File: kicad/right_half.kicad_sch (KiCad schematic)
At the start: 50 parts, among them J10 Conn_01x03_Pin, J3 AudioJack4, J4 Conn_01x04_Pin, J9 Conn_01x04_Pin, SW19 SW_Push, SW20 SW_Push, SW21 SW_Push, SW22 SW_Push, SW23 SW_Push, SW24 SW_Push, SW25 SW_Push, SW26 SW_Push, SW27 SW_Push, SW28 SW_Push, SW29 SW_Push, SW30 SW_Push, SW31 SW_Push, SW32 SW_Push, SW33 SW_Push, U2 RP2040-Zero

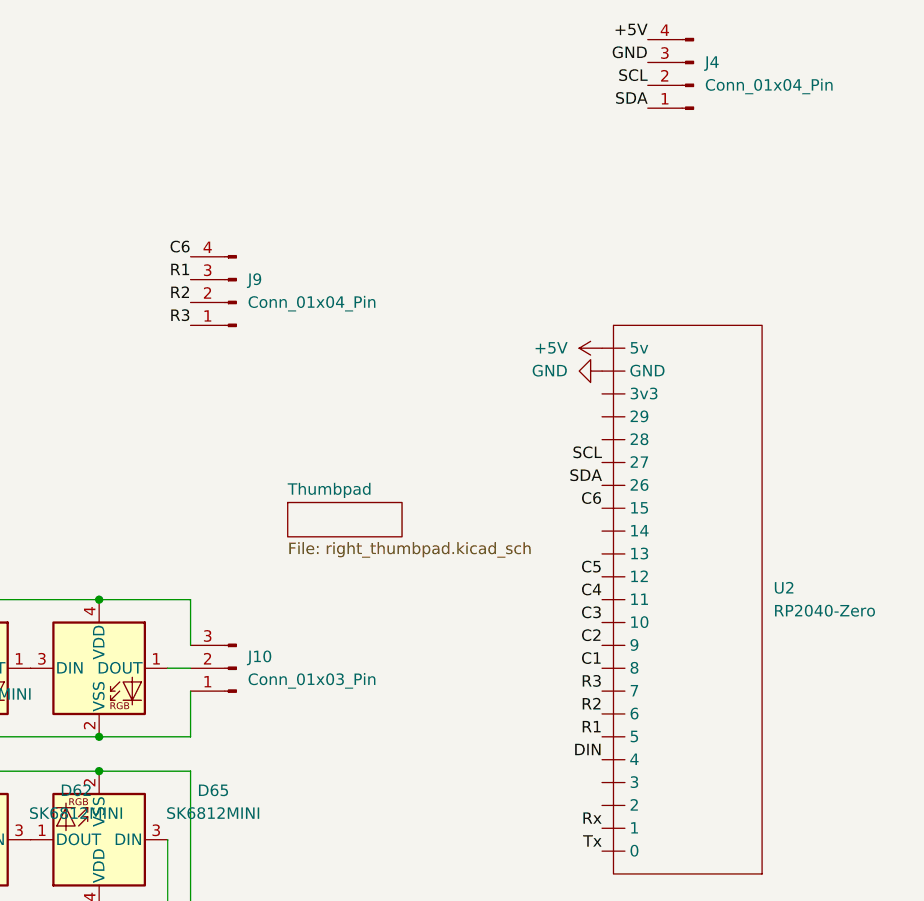
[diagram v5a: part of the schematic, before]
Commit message: final PCB ready
- bugs: LED position and wiring (wrong by footprint)
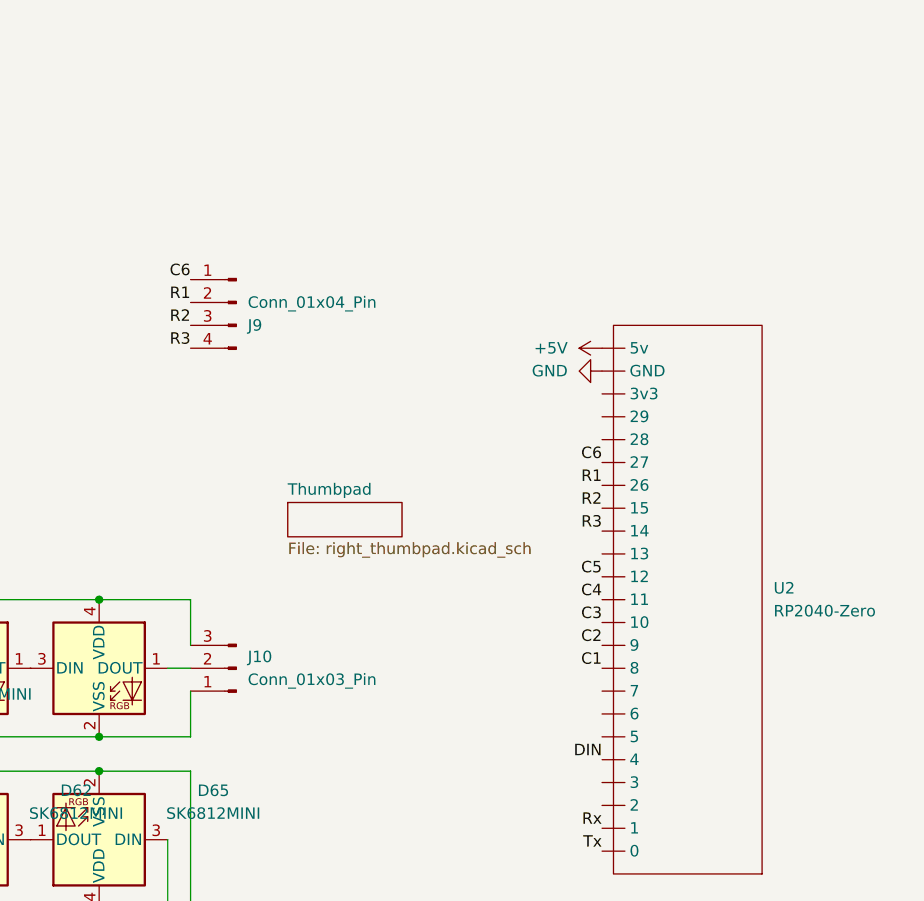
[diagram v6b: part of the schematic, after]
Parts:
- removed J4: Conn_01x04_Pin, Connector_PinHeader_2.54mm:PinHeader_1x04_P2.54mm_Vertical, symbol Connector:Conn_01x04_Pin
- J10: footprint Connector_PinSocket_2.54mm:PinSocket_1x03_P2.54mm_Vertical -> pogo-socket-angled:PinSocket_1x03_P2.54mm_Vertical
- J9: footprint Connector_PinSocket_2.54mm:PinSocket_1x04_P2.54mm_Vertical -> pogo-socket-angled:PinSocket_1x04_P2.54mm_Vertical
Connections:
- net SCL is gone; now on net C6: U2.27
- net SDA is gone; now on net R1: U2.26
- net C6: now also J9.1 (Pin_1); no longer J9.4 (Pin_4), U2.15
- net R1: now also J9.2 (Pin_2); no longer J9.3 (Pin_3), U2.5
- net R2: now also J9.3 (Pin_3), U2.15; no longer J9.2 (Pin_2), U2.6
- net R3: now also J9.4 (Pin_4), U2.14; no longer J9.1 (Pin_1), U2.7
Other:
- moved on the sheet: J9
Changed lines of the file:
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@@
 		)
 	)
-	(label "SDA"
-		(at 241.3 41.91 180)
-		(effects
-			(font
-				(size 1.27 1.27)
-			)
-			(justify right bottom)
-		)
-	)
 	(label "GND"
 		(at 187.96 135.89 0)
@@
 	)
 	(label "R2"
-		(at 236.22 109.22 180)
+		(at 236.22 86.36 180)
 		(effects
 			(font
@@
 	)
 	(label "C6"
-		(at 236.22 86.36 180)
+		(at 236.22 81.28 180)
 		(effects
 			(font
@@
 	)
 	(label "R1"
-		(at 190.5 60.96 180)
+		(at 190.5 63.5 180)
 		(effects
 			(font
@@
 		)
 	)
-	(label "+5V"
-		(at 241.3 34.29 180)
-		(effects
-			(font
-				(size 1.27 1.27)
-			)
-			(justify right bottom)
-		)
-	)
 	(label "R3"
-		(at 190.5 66.04 180)
+		(at 190.5 68.58 180)
 		(effects
 			(font
@@
 		)
 	)
-	(label "GND"
-		(at 241.3 36.83 180)
-		(effects
-			(font
-				(size 1.27 1.27)
-			)
-			(justify right bottom)
-		)
-	)
 	(label "R2"
 		(at 116.84 71.12 0)
@@
 	)
 	(label "R2"
-		(at 190.5 63.5 180)
-		(effects
-			(font
-				(size 1.27 1.27)
-			)
-			(justify right bottom)
-		)
-	)
-	(label "SDA"
-		(at 236.22 83.82 180)
+		(at 190.5 66.04 180)
 		(effects
 			(font
@@
 	)
 	(label "R3"
-		(at 236.22 106.68 180)
+		(at 236.22 88.9 180)
 		(effects
 			(font
@@
 	)
 	(label "R1"
-		(at 236.22 111.76 180)
+		(at 236.22 83.82 180)
 		(effects
 			(font
@@
 		)
 	)
-	(label "SCL"
-		(at 241.3 39.37 180)
-		(effects
-			(font
-				(size 1.27 1.27)
-			)
-			(justify right bottom)
-		)
-	)
 	(label "Rx"
 		(at 236.22 121.92 180)
@@
 	)
 	(label "C6"
-		(at 190.5 58.42 180)
+		(at 190.5 60.96 180)
 		(effects
 			(font
@@
 		)
 	)
-	(label "SCL"
-		(at 236.22 81.28 180)
-		(effects
-			(font
-				(size 1.27 1.27)
-			)
-			(justify right bottom)
-		)
-	)
 	(label "R1"
 		(at 97.79 52.07 0)
@@
 	(symbol
 		(lib_id "Connector:Conn_01x04_Pin")
-		(at 195.58 63.5 180)
+		(at 195.58 63.5 0)
+		(mirror y)
 		(unit 1)
 		(exclude_from_sim no)
@@
 		(fields_autoplaced yes)
 		(property "Reference" "J9"
-			(at 196.85 60.9599 0)
+			(at 196.85 66.0401 0)
 			(effects
 				(font
@@
 		)
 		(property "Value" "Conn_01x04_Pin"
-			(at 196.85 63.4999 0)
+			(at 196.85 63.5001 0)
 			(effects
 				(font
@@
 			)
 		)
-		(property "Footprint" "Connector_PinSocket_2.54mm:PinSocket_1x04_P2.54mm_Vertical"
+		(property "Footprint" "pogo-socket-angled:PinSocket_1x04_P2.54mm_Vertical"
 			(at 195.58 63.5 0)
 			(effects
@@
 	)
 	(symbol
-		(lib_id "Connector:Conn_01x04_Pin")
-		(at 246.38 39.37 180)
-		(unit 1)
-		(exclude_from_sim no)
-		(in_bom yes)
-		(on_board yes)
-		(dnp no)
-		(fields_autoplaced yes)
-		(property "Reference" "J4"
-			(at 247.65 36.8299 0)
-			(effects
-				(font
-					(size 1.27 1.27)
-				)
-				(justify right)
-			)
-		)
-		(property "Value" "Conn_01x04_Pin"
-			(at 247.65 39.3699 0)
-			(effects
-				(font
-					(size 1.27 1.27)
-				)
-				(justify right)
-			)
-		)
-		(property "Footprint" "Connector_PinHeader_2.54mm:PinHeader_1x04_P2.54mm_Vertical"
-			(at 246.38 39.37 0)
-			(effects
-				(font
-					(size 1.27 1.27)
-				)
-				(hide yes)
-			)
-		)
-		(property "Datasheet" "~"
-			(at 246.38 39.37 0)
-			(effects
-				(font
-					(size 1.27 1.27)
-				)
-				(hide yes)
-			)
-		)
-		(property "Description" "Generic connector, single row, 01x04, script generated"
-			(at 246.38 39.37 0)
-			(effects
-				(font
-					(size 1.27 1.27)
-				)
-				(hide yes)
-			)
-		)
-		(pin "4"
-		)
-		(pin "2"
-		)
-		(pin "3"
-		)
-		(pin "1"
-		)
-		(instances
-			(project ""
-				(path "/de3a30da-dd56-4801-a3f5-765b04aa12e1/d777195d-63e1-45cf-bdcd-083236482c4e"
-					(reference "J4")
-					(unit 1)
-				)
-			)
-		)
-	)
-	(symbol
 		(lib_id "Device:D")
 		(at 116.84 48.26 90)
@@
 			)
 		)
-		(property "Footprint" "Connector_PinSocket_2.54mm:PinSocket_1x03_P2.54mm_Vertical"
+		(property "Footprint" "pogo-socket-angled:PinSocket_1x03_P2.54mm_Vertical"
 			(at 195.58 104.14 0)
 			(effects
